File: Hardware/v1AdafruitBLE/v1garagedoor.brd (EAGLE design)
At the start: 85 x 59.7 mm, 27 parts, among them IC1 78V, Q1 2N3904, U1 ATMEGA328P_PDIP, X1 16mhz

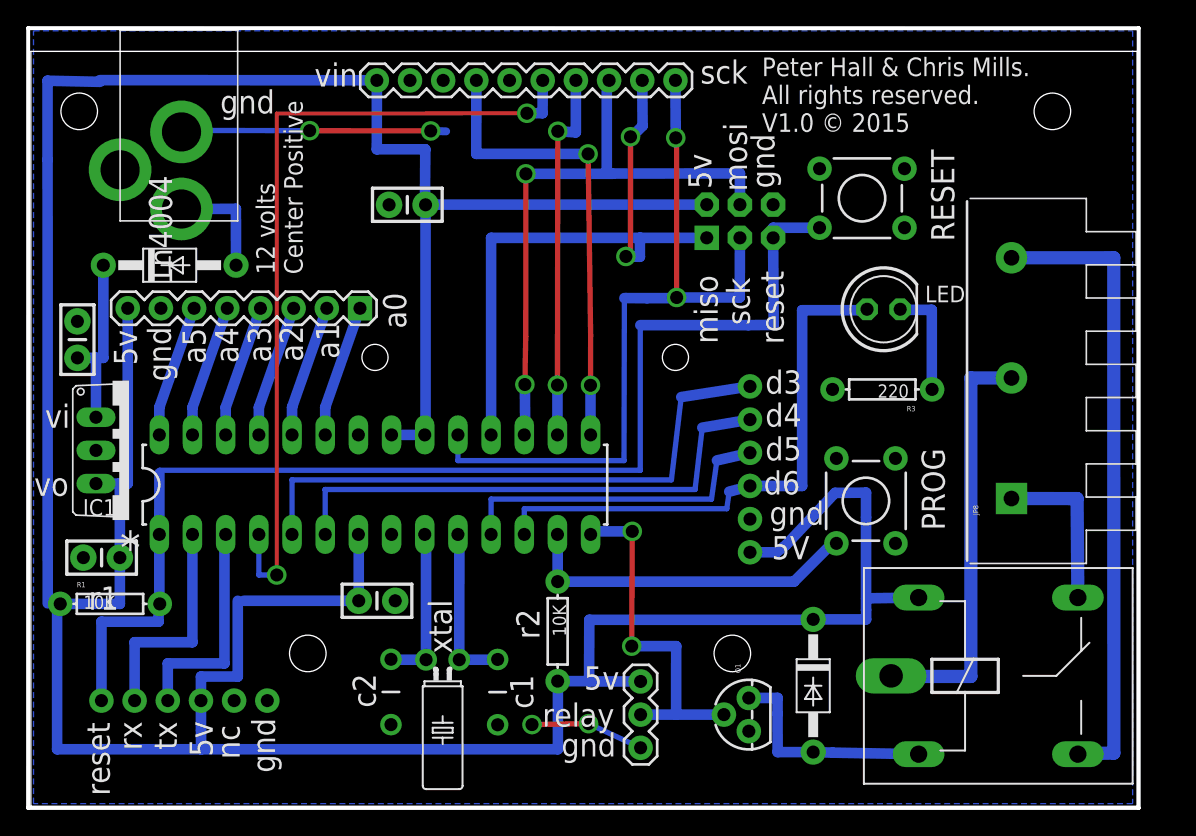
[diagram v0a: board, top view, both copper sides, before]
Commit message: added some documentation made some changes to the board layout because of the v1 board has some needed changes. I expect there to be a few more changes, around the silkscreen output
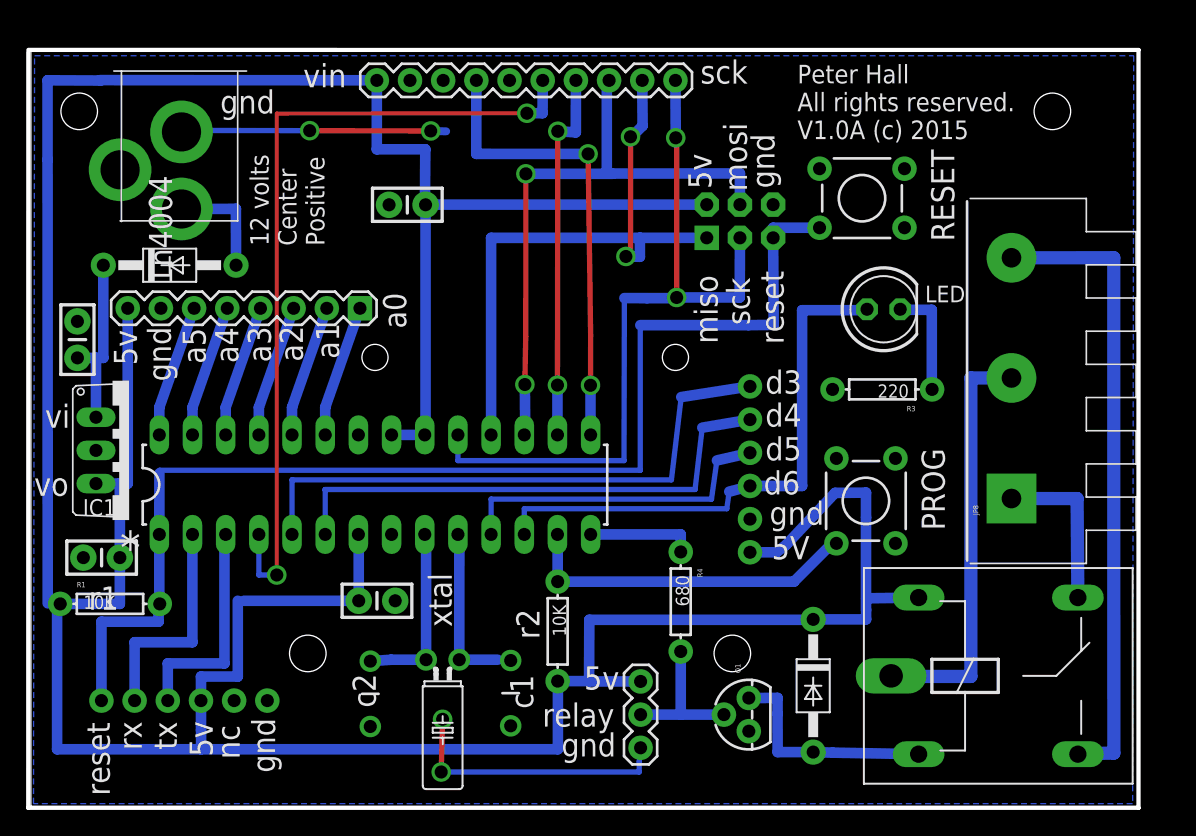
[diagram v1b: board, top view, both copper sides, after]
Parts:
- added R4: 680, SparkFun-Resistors:AXIAL-0.3
- moved C2 1.59 mm to (26.2, 8.82)
- moved C1 1.00 mm to (36.9, 8.87)
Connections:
- new net N$7: R4.P$1, U1.14
- net RELAY: now also R4.P$2; no longer U1.14
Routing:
- net RELAY: track 27.3 -> 11.2 mm, vias 2 -> 0
- net GND: track 29.4 -> 41.8 mm
- net N$7: track 0.00 -> 8.24 mm
- net N$1: track 12.4 -> 14.0 mm
- net N$2: track 12.7 -> 13.6 mm
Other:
- board size 85 x 59.7 mm -> 85 x 58 mm
- board text added: "Peter Hall All rights reserved. V1.0A (c) 2015"
- board text removed: "Peter Hall & Chris Mills. All rights reserved. V1.0 © 2015"

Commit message: just updating the repo
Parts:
- C1, C2: value 20pF -> 33pF
- C6, C7: value .33uF -> .1uF
- JP4: value test point relay -> (none)
- R4: value 680 -> 2K4
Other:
- board text added: "0.1uF"
- board text added: "9 volts Center Positive"
- board text added: "All rights reserved (c) Peter Hall V1.0A 2016"
- board text removed: "12 volts Center Positive"
- board text removed: "1n4004"
- board text removed: "Peter Hall All rights reserved. V1.0A (c) 2015"
- board text removed: "r1"
- board text removed: "r2"
